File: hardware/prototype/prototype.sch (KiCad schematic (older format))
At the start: 67 parts, among them J1 Jack-DC, J2 0734120114, J3 Conn_01x04, J4 Conn_01x04, J5 Conn_02x07_Odd_Even, J6 Battery-holder, J7 Conn_02x12_Odd_Even, Q1 Si2323, U1 QUECTEL_L80, U2 TLV71333PDBV, U3 LM2596_MODULE, U4 DevkitC, U5 MIKROE_3G_CLICK

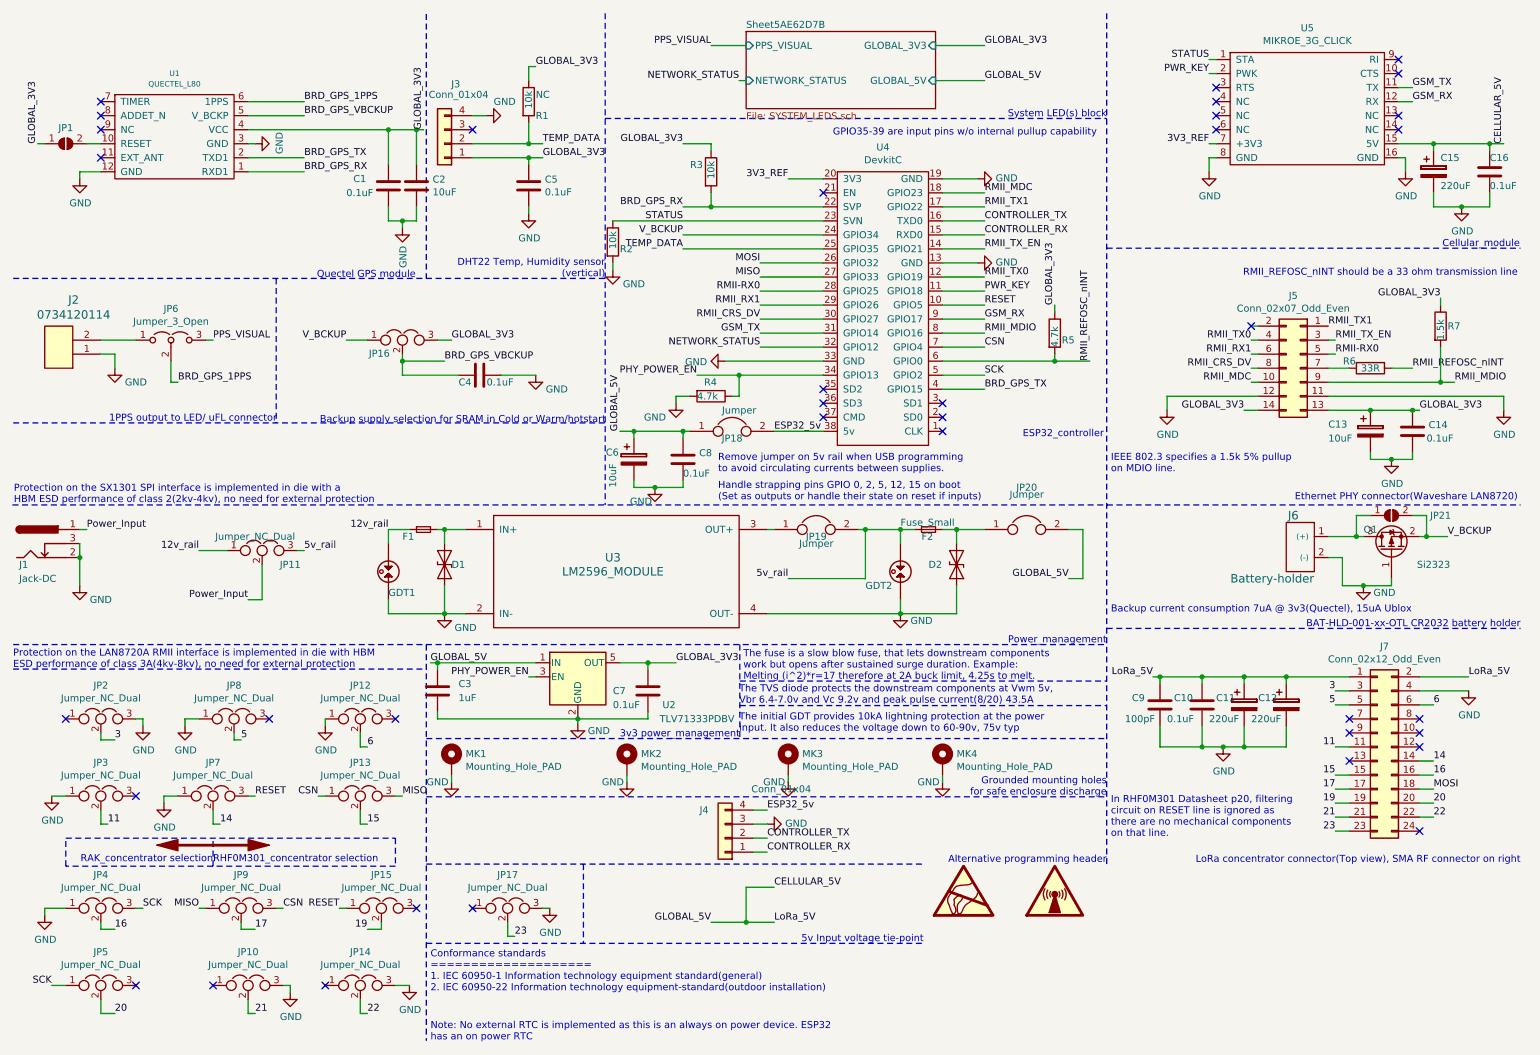
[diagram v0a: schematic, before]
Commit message: Complete PCB design, BOM generation and gerber generation
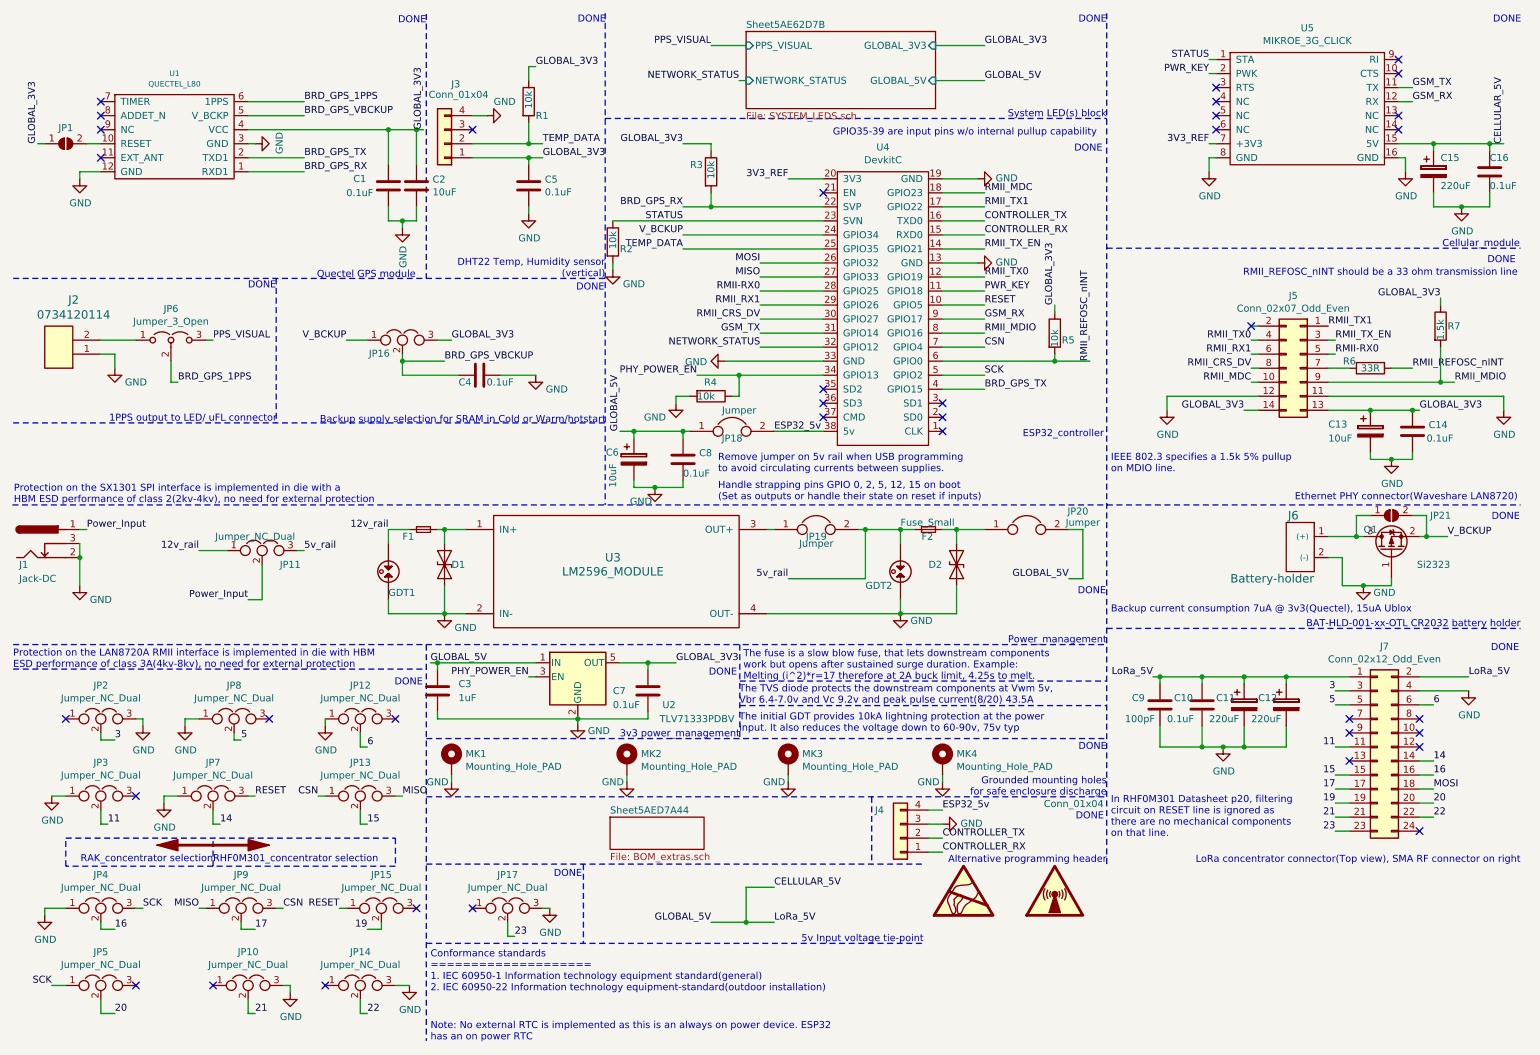
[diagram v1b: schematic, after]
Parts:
- C1, C5: manf# (none) -> GCM21BR72A104KA37K; purchase_page (none) -> https://www.digikey.com/product-detail/en/murata-electronic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
- C10, C14, C16, C4, C7, C8: manf# (none) -> GCM21BR72A104KA37K
- C11, C12, C15: manf# (none) -> UUD0J221MCL1GS
- C13, C6: manf# (none) -> C2012X5R1E106M085AC
- C2: manf# (none) -> C2012X5R1E106M085AC; purchase page https://www.digikey.com/product-detail/en/avx-corporation/T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 -> https://www.digikey.com/product-detail/en/murata-electronic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
- C3: manf# (none) -> CC0805KKX7R7BB105
- C9: manf# (none) -> 06035A101FAT2A
- D1, D2: manf# (none) -> SMA6J12A
- F1, F2: manf# (none) -> 0461002.ER
- GDT1, GDT2: manf# (none) -> SL1411A075SM; purchase page https://www.digikey.com/product-detail/en/littelfuse-inc/SL1411A075A/F5590CT-ND/3307063 -> https://www.digikey.com/product-detail/en/littelfuse-inc/SL1411A075SM/F10923CT-ND/8109613
- J1: manf# (none) -> PJ-002A
- J2: manf# (none) -> 0734120114
- J3: manf# (none) -> 1528-1504-ND; purchase_page (none) -> https://www.digikey.com/product-detail/en/sullins-connector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
- J4: manf# (none) -> 801-43-050-10-001000; purchase_page (none) -> https://www.digikey.com/product-detail/en/mill-max-manufact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
- J6: manf# (none) -> BAT-HLD-001
- JP10, JP11, JP12, JP13, JP14, JP15, JP16, JP17, JP2, JP3, JP4, JP5, JP7, JP8, JP9: manf# (none) -> 61300311121
- JP18, JP19, JP20: manf# (none) -> 61300211121
- JP6: manf# (none) -> 61300311121; purchase_page (none) -> https://www.digikey.com/product-detail/en/wurth-electronics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
- Q1: manf# (none) -> SI2323CDS-T1-GE3
- R1: Population status NC -> (none); manf# (none) -> RR1220P-103-D; purchase_page (none) -> https://www.digikey.com/product-detail/en/susumu/RR1220P-10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
- R2, R3: manf# (none) -> RR1220P-103-D
- R4, R5: value 4.7k -> 10k; manf# (none) -> RR1220P-103-D
- R6: manf# (none) -> RC0805FR-0733RL; purchase_page (none) -> https://www.digikey.com/product-detail/en/yageo/RC0805FR-07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
- R7: manf# (none) -> ESR10EZPJ152; purchase_page (none) -> https://www.digikey.com/product-detail/en/rohm-semiconducto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
- U2: manf# (none) -> TLV73333PDBVR
- U4: manf# (none) -> ESP32-DEVKITC; purchase page https://www.digikey.com/product-detail/en/espressif-systems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 -> (none); purchase_page (none) -> https://gridconnect.com/esp-devkitc-wifi-module-esp32-devel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
- U5: manf# (none) -> MIKROE-2226
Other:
- note added: "DONE"
- moved on the sheet: J4

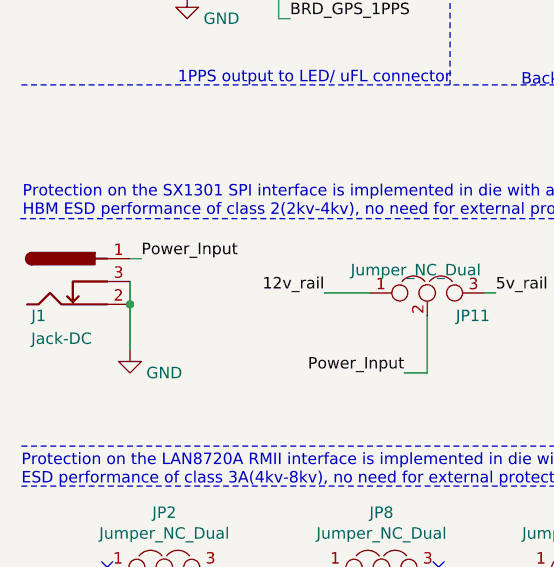
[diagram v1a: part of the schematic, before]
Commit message: Add main file
1. Update README
2. Add BOM
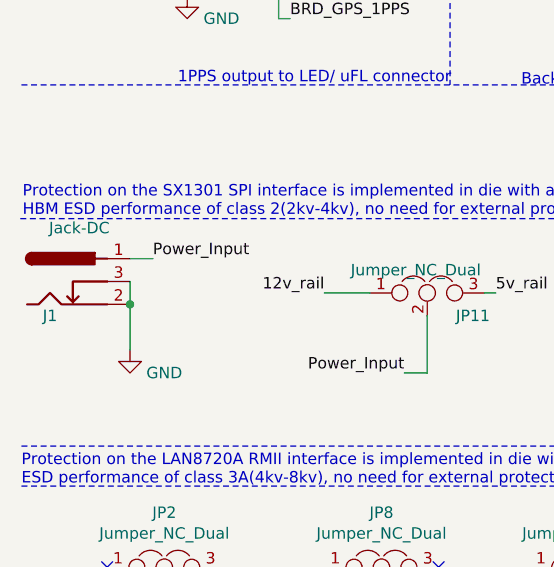
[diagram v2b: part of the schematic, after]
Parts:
- removed J1: Jack-DC, Connector_BarrelJack:BarrelJack_Horizontal, symbol Connector_Specialized:Jack-DC
- added J1: Jack-DC, symbol Connector:Jack-DC
- C1, C5: manf# GCM21BR72A104KA37K -> CGA4J2X7R2A104K125AA; purchase_page https://www.digikey.com/product-detail/en/murata-electronics-north-america/GCM21BR72A104KA37K/490-8051-1-ND/4380336 -> https://www.digikey.com/product-detail/en/murata-electronics-north-america/GCM21BR72A104KA37L/490-4789-1-ND/1641708
- C10, C14, C16, C4, C7, C8: manf# GCM21BR72A104KA37K -> CGA4J2X7R2A104K125AA
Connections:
- net GND: now also J1.2, J1.3
- net Power_Input: now also J1.1
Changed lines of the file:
@@
 F 2 "Capacitor_SMD:C_0805_2012Metric_Pad1.15x1.50mm_HandSolder" H 4188 1550 50  0001 C CNN
 F 3 "http://psearch.en.murata.com/capacitor/product/GCM21BR72A104KA37%23.pdf" H 4150 1700 50  0001 C CNN
-F 4 "https://www.digikey.com/product-detail/en/murata-electronics-north-america/GCM21BR72A104KA37K/490-8051-1-ND/4380336" H 4150 1700 50  0001 C CNN "purchase_page"
-F 5 "GCM21BR72A104KA37K " H 4150 1700 50  0001 C CNN "manf#"
+F 4 "https://www.digikey.com/product-detail/en/murata-electronics-north-america/GCM21BR72A104KA37L/490-4789-1-ND/1641708" H 4150 1700 50  0001 C CNN "purchase_page"
+F 5 "CGA4J2X7R2A104K125AA " H 4150 1700 50  0001 C CNN "manf#"
 	1    4150 1700
 	1    0    0    -1
@@
 F 2 "Capacitor_SMD:C_0805_2012Metric_Pad1.15x1.50mm_HandSolder" H 3838 2900 50  0001 C CNN
 F 3 "~" H 3800 3050 50  0001 C CNN
-F 4 "GCM21BR72A104KA37K " V 3800 3050 50  0001 C CNN "manf#"
+F 4 "CGA4J2X7R2A104K125AA " V 3800 3050 50  0001 C CNN "manf#"
 	1    3800 3050
 	0    1    1    0
@@
 F 2 "Capacitor_SMD:C_0805_2012Metric_Pad1.15x1.50mm_HandSolder" H 5038 5150 50  0001 C CNN
 F 3 "~" H 5000 5300 50  0001 C CNN
-F 4 "GCM21BR72A104KA37K" H 5000 5300 50  0001 C CNN "manf#"
+F 4 "CGA4J2X7R2A104K125AA " H 5000 5300 50  0001 C CNN "manf#"
 	1    5000 5300
 	1    0    0    -1
@@
 F 2 "Capacitor_SMD:C_0805_2012Metric_Pad1.15x1.50mm_HandSolder" H 11038 1450 50  0001 C CNN
 F 3 "~" H 11000 1600 50  0001 C CNN
-F 4 "GCM21BR72A104KA37K " H 11000 1600 50  0001 C CNN "manf#"
+F 4 "CGA4J2X7R2A104K125AA " H 11000 1600 50  0001 C CNN "manf#"
 	1    11000 1600
 	1    0    0    -1
@@
 F 2 "Capacitor_SMD:C_0805_2012Metric_Pad1.15x1.50mm_HandSolder" H 5288 3500 50  0001 C CNN
 F 3 "~" H 5250 3650 50  0001 C CNN
-F 4 "GCM21BR72A104KA37K " H 5250 3650 50  0001 C CNN "manf#"
+F 4 "CGA4J2X7R2A104K125AA " H 5250 3650 50  0001 C CNN "manf#"
 	1    5250 3650
 	1    0    0    -1
@@
 F 2 "Capacitor_SMD:C_0805_2012Metric_Pad1.15x1.50mm_HandSolder" H 3188 1550 50  0001 C CNN
 F 3 "https://psearch.en.murata.com/capacitor/product/GCM21BR72A104KA37%23.pdf" H 3150 1700 50  0001 C CNN
-F 4 "https://www.digikey.com/product-detail/en/murata-electronics-north-america/GCM21BR72A104KA37K/490-8051-1-ND/4380336" H 3150 1700 50  0001 C CNN "purchase_page"
-F 5 "GCM21BR72A104KA37K " H 3150 1700 50  0001 C CNN "manf#"
+F 4 "https://www.digikey.com/product-detail/en/murata-electronics-north-america/GCM21BR72A104KA37L/490-4789-1-ND/1641708" H 3150 1700 50  0001 C CNN "purchase_page"
+F 5 "CGA4J2X7R2A104K125AA " H 3150 1700 50  0001 C CNN "manf#"
 	1    3150 1700
 	1    0    0    -1
@@
 F 2 "Capacitor_SMD:C_0805_2012Metric_Pad1.15x1.50mm_HandSolder" H 10488 3300 50  0001 C CNN
 F 3 "~" H 10450 3450 50  0001 C CNN
-F 4 "GCM21BR72A104KA37K" H 10450 3450 50  0001 C CNN "manf#"
+F 4 "CGA4J2X7R2A104K125AA " H 10450 3450 50  0001 C CNN "manf#"
 	1    10450 3450
 	1    0    0    -1
@@
 Text Notes 2355 3390 2    50   ~ 0
 1PPS output to LED/ uFL connector
-$Comp
-L Connector_Specialized:Jack-DC J1
-U 1 1 5B03C5B5
-P 650 4250
-F 0 "J1" H 550 4100 50  0000 C CNN
-F 1 "Jack-DC" H 650 4000 50  0000 C CNN
-F 2 "Connector_BarrelJack:BarrelJack_Horizontal" H 700 4210 50  0001 C CNN
-F 3 "https://www.cui.com/product/resource/pj-002a.pdf" H 700 4210 50  0001 C CNN
-F 4 "https://www.digikey.com/product-detail/en/cui-inc/PJ-002A/CP-002A-ND/96962" H 650 4250 50  0001 C CNN "purchase page"
-F 5 "PJ-002A" H 650 4250 50  0001 C CNN "manf#"
-	1    650  4250
-	1    0    0    -1
-$EndComp
 Text Label 5900 3450 0    50   ~ 0
 ESP32_5v
@@
 F 2 "Capacitor_SMD:C_0805_2012Metric_Pad1.15x1.50mm_HandSolder" H 8988 5250 50  0001 C CNN
 F 3 "~" H 8950 5400 50  0001 C CNN
-F 4 "GCM21BR72A104KA37K" H 8950 5400 50  0001 C CNN "manf#"
+F 4 "CGA4J2X7R2A104K125AA " H 8950 5400 50  0001 C CNN "manf#"
 	1    8950 5400
 	1    0    0    -1
@@
 	3550 4550 3550 4750
 Connection ~ 3550 4750
-Wire Wire Line
-	950  4250 950  4350
 Wire Wire Line
 	5850 4750 6800 4750
@@
 $EndComp
 Wire Wire Line
-	950  4150 1000 4150
-Text Label 1000 4150 0    50   ~ 0
+	950  4150 1050 4150
+Text Label 1050 4150 0    50   ~ 0
 Power_Input
 $Comp
@@
 	1    0    0    -1
 $EndComp
-Wire Wire Line
-	950  4550 950  4350
-Connection ~ 950  4350
 Text Label 2150 4650 2    50   ~ 0
 Power_Input
@@
 Text Notes 8250 6225 2    50   ~ 0
 DONE
+Wire Wire Line
+	950  4250 950  4350
+$Comp
+L Connector:Jack-DC J1
+U 1 1 5AF61C3C
+P 650 4250
+F 0 "J1" H 600 4100 50  0000 C CNN
+F 1 "Jack-DC" H 728 4484 50  0000 C CNN
+F 2 "" H 700 4210 50  0001 C CNN
+F 3 "~" H 700 4210 50  0001 C CNN
+F 4 "PJ-002A " H 650 4250 50  0001 C CNN "manf#"
+	1    650  4250
+	1    0    0    -1
+$EndComp
+Wire Wire Line
+	950  4350 950  4550
+Connection ~ 950  4350
 $EndSCHEMATC
